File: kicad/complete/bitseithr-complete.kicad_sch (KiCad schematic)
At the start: 58 parts, among them CN1 SHIELD CONN 2, CN10 SHIELD CONN 3, CN11 SHIELD CONN 4, CN12 SHIELD CONN 5, CN2 SHIELD CONN 7, CN3 SHIELD CONN 8, CN4 PIGTAIL 4, CN5 PIGTAIL 3, CN6 PIGTAIL 5, CN7 PIGTAIL 1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

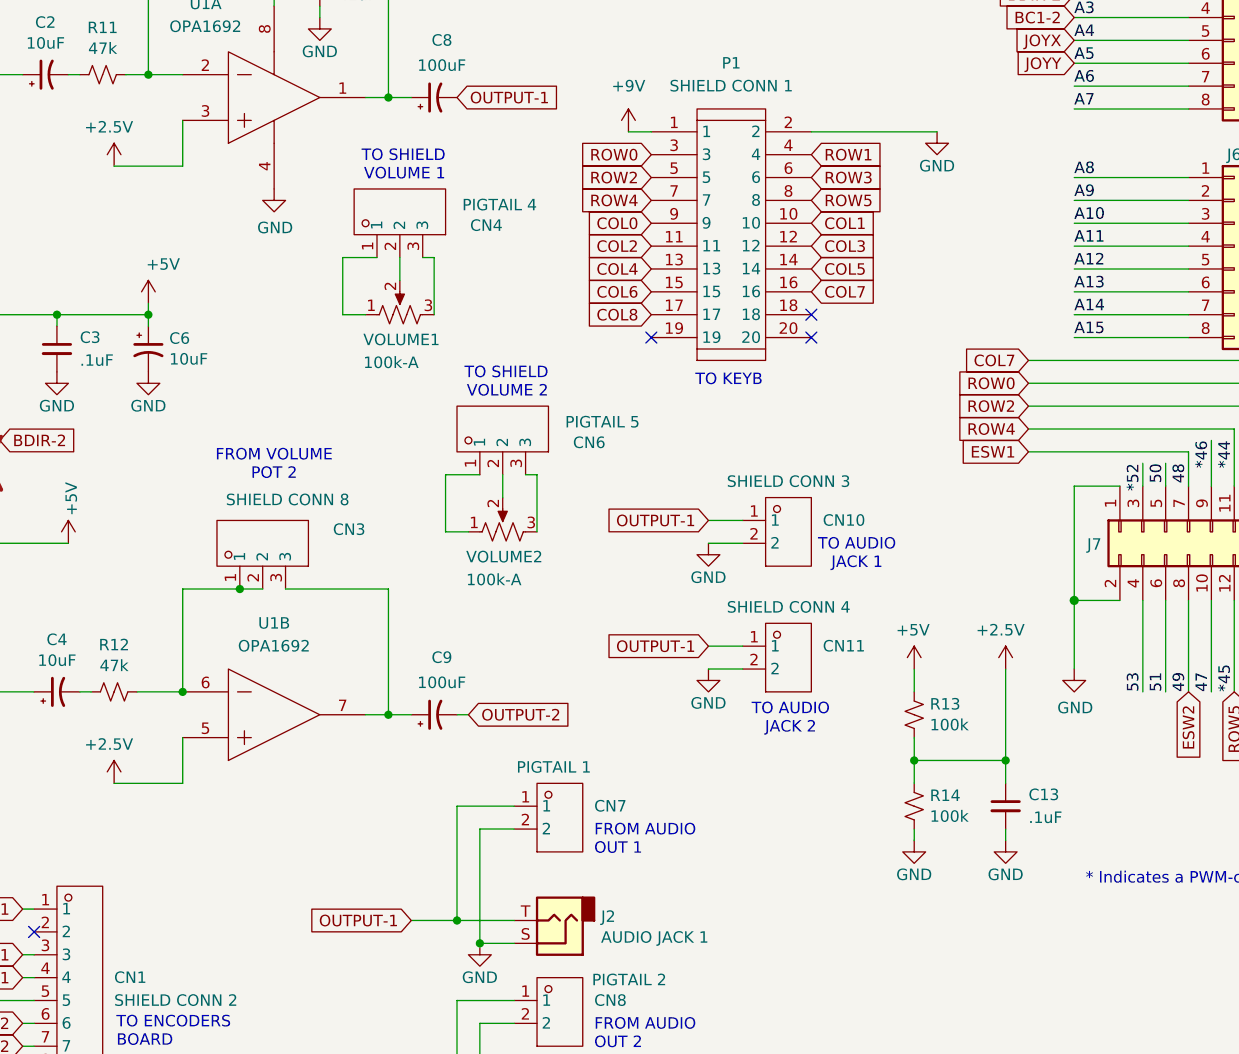
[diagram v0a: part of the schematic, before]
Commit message: minor revisions to the op-amp sections
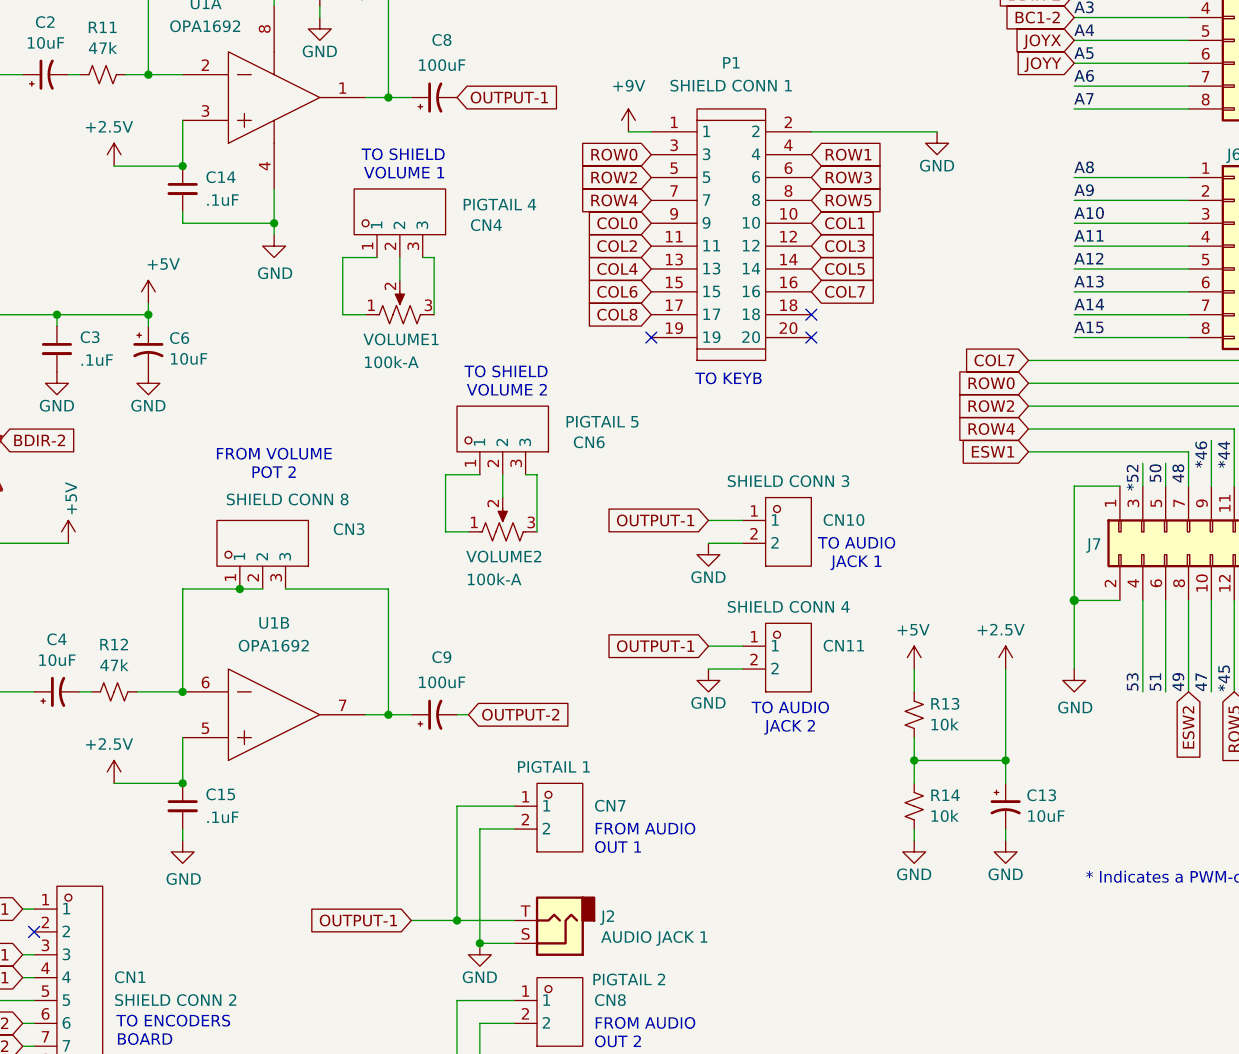
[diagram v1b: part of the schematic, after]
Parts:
- removed C13: .1uF, symbol Device:C_Small
- added C13: 10uF, Capacitor_THT:CP_Radial_D5.0mm_P2.50mm, symbol Device:C_Polarized_Small_US
- added C14, C15: .1uF, symbol Device:C_Small
- R13, R14: value 100k -> 10k
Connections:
- net +2.5V: now also C13.1, C14.1, C15.1
- net GND: now also C13.2, C14.2, C15.2
